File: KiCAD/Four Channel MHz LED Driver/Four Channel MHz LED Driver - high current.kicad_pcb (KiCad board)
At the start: 2 copper layers, 100 x 126 mm, 88 parts, among them J10 Conn_01x24_Female, J2 Conn_01x02_Female, J3 8P8C_Shielded_x4, J4 Conn_01x03_Male, J5 Conn_01x03_Female, J6 Conn_01x08_Female, J7 Conn_01x03_Female, J8 Conn_01x05_Female, J9 Conn_01x24_Female, M1 Fan_4pin, Q1 SUM70060E, SW1 Pushbutton_with_LED, SW2 Pushbutton_with_LED, SW3 Pushbutton_with_LED, SW4 Pushbutton_with_LED, SW5 SW_SPDT, U1 12V boost, U12 Teensy3.6, U2 SN74LV4T125PWR, U3 DPBW06F-05, U4 TMUX1204DGSR, U5 HTSOP-J8_ROM, U6 ADP7182AUJZ-1.8-R7, U7 LT6200CS8-10

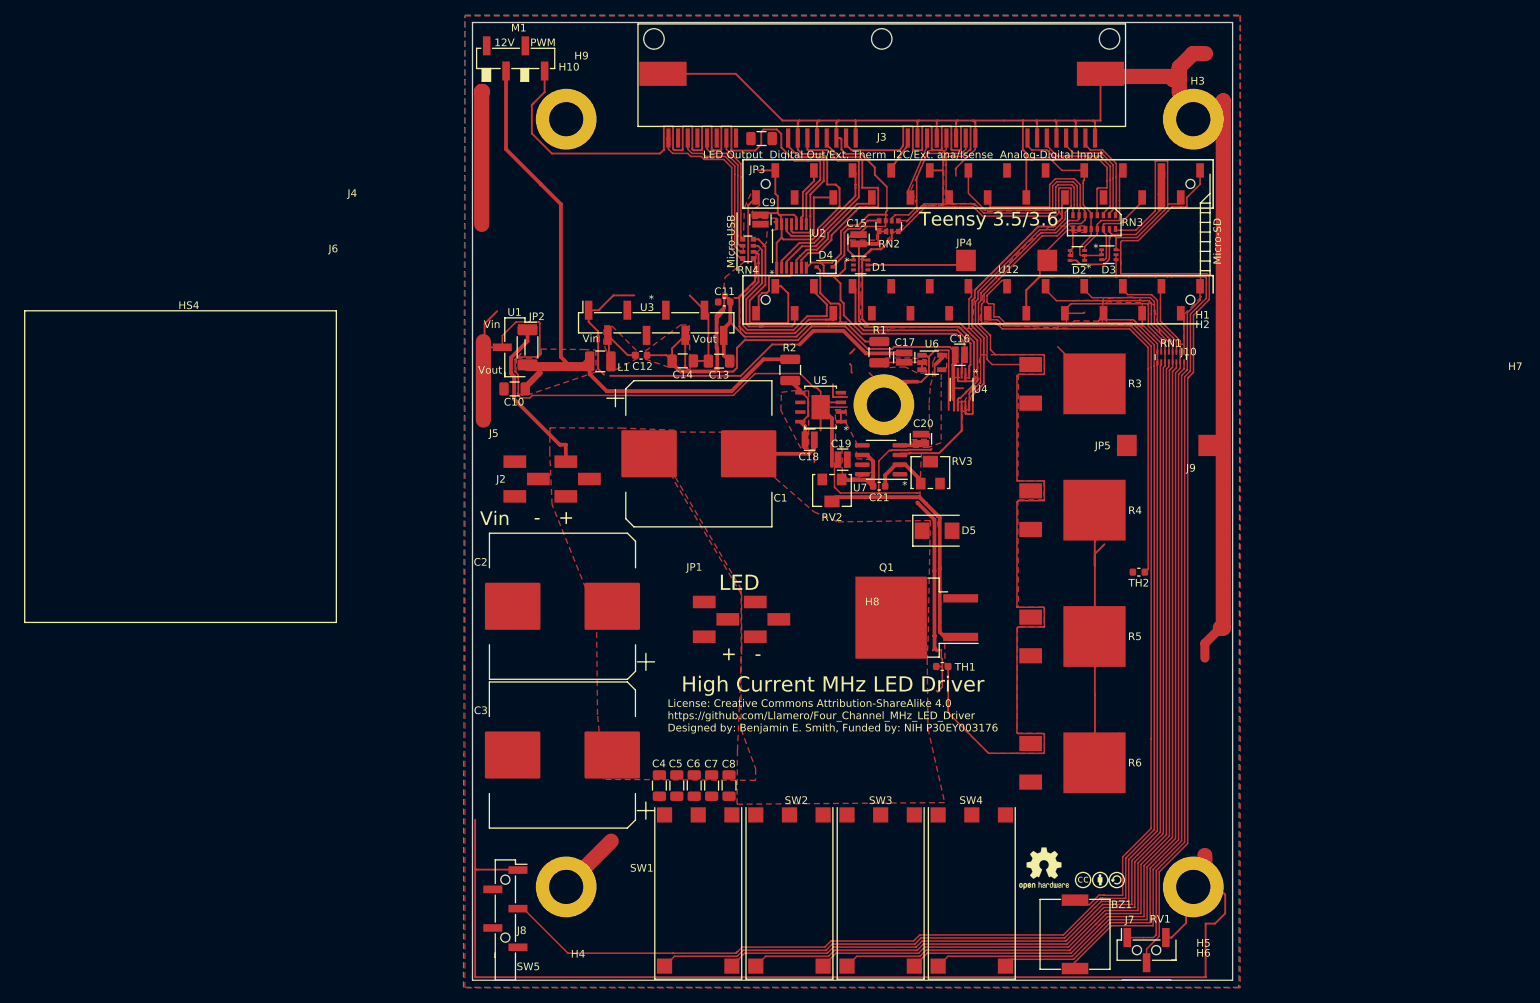
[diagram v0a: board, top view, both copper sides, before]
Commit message: Updated layout - still need to update resistors
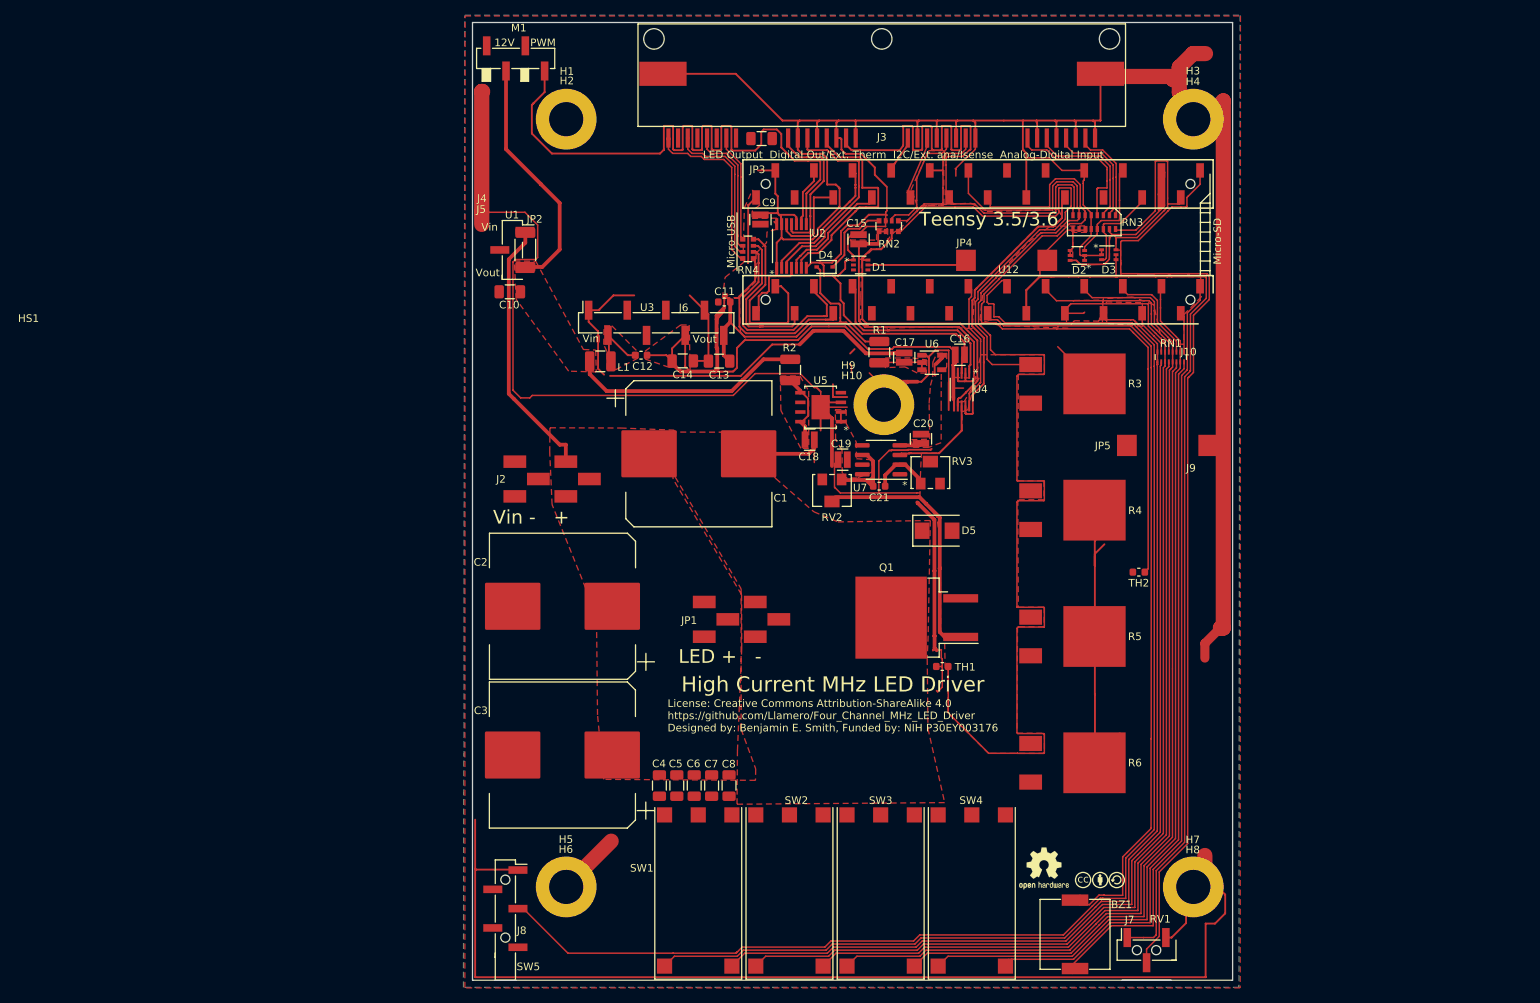
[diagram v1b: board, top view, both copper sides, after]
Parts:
- removed the HS1 at (112.1, 137.1)
- removed HS2, HS3: HS-PCB, Custom Footprints:Heatsink_910-40-2-23-2-B-0
- HS1: renamed from HS4; footprint Custom Footprints:Heatsink_910-40-2-23-2-B-0 -> Custom Footprints:Ref_only
- moved JP2 12.8 mm to (60.2, 78.5)
- moved U1 12.8 mm to (58.5, 78.5)
- moved C10 12.8 mm to (58.1, 84.0)
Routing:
- net /12V: track 92.0 -> 66.1 mm
- net /Vin: track 22.8 -> 34.6 mm
- net GND: track 881.5 -> 873.4 mm
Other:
- board text added: "LED + -"
- board text added: "Vin - +"
- board text removed: "+ -"
- board text removed: "- +"
- board text removed: "LED"
- board text removed: "Vin"
